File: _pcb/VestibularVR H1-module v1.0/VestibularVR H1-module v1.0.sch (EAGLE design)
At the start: 67 parts, among them IC1 FT232RL, IC2 74LVC1G07DBV, IC3 LP5907MFX-3.3, IC4 74LVC1G07DBV, IC5 74LVC1G07DBV, IC6 74LVC1G07DBV, IC7 USBLC6-2SC6, IC8 ATXMEGA32A4U, T1 DMG1012UW, T2 DMG1012UW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

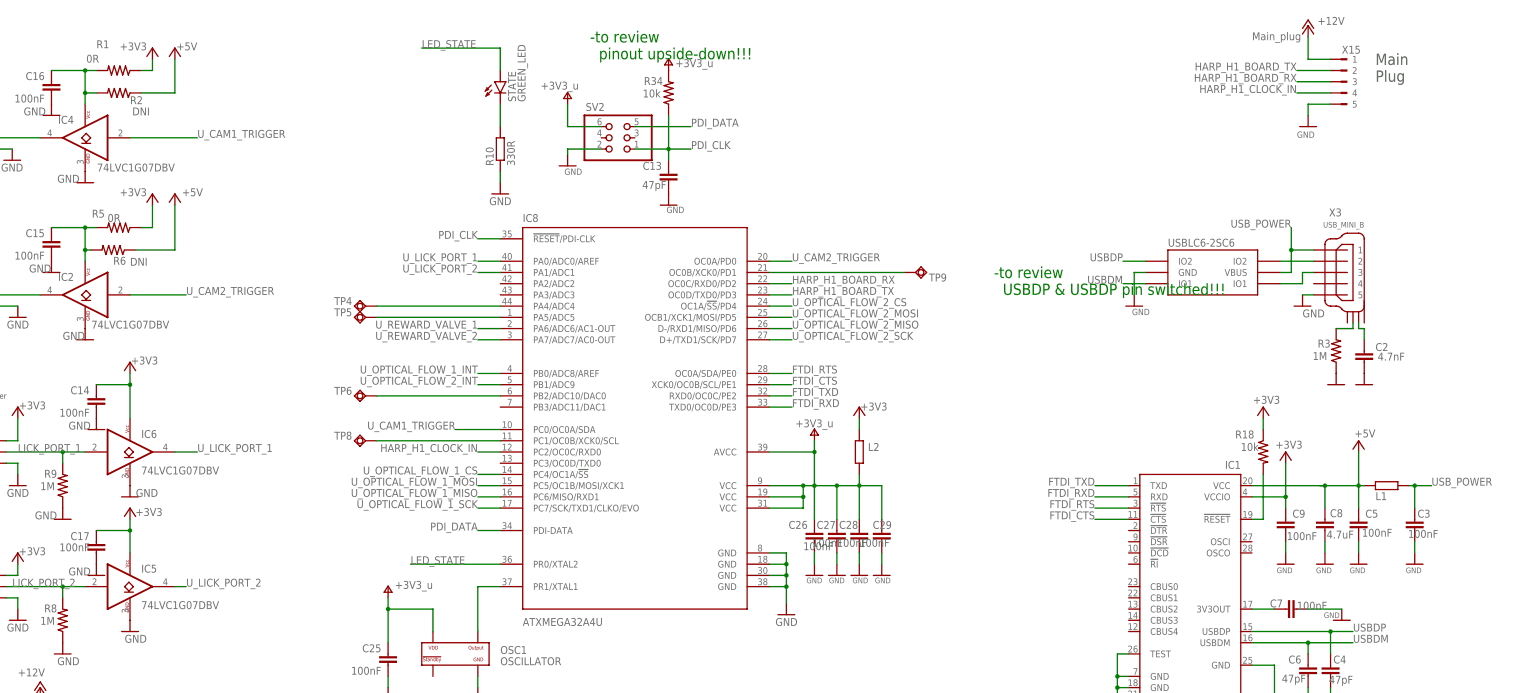
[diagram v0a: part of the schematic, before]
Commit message: VestibularVR H1BOM updates & Lick Sensor step on
- VestibularVR H1
. component ref updated
. BOM file updated

- Lick Sensor module v1.0
. still only on schematic design
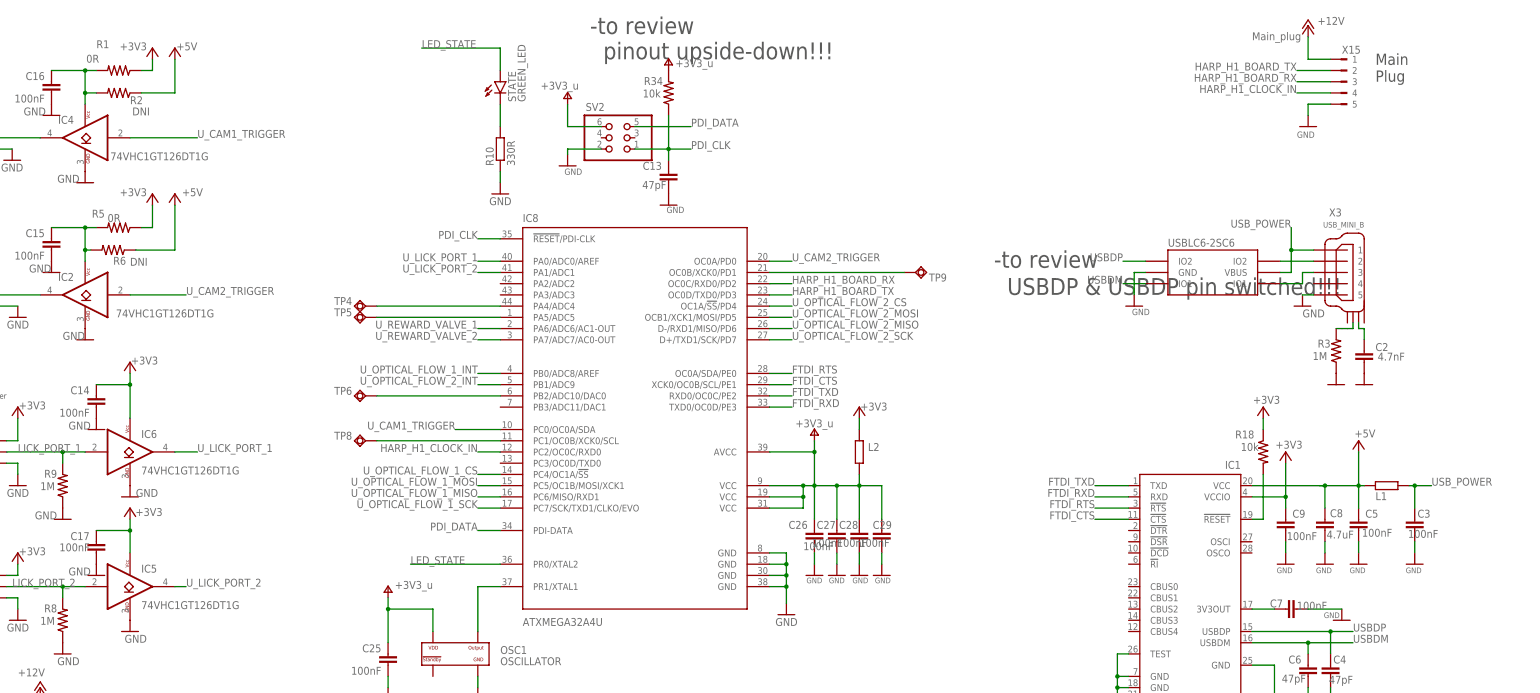
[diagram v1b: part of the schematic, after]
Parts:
- IC2, IC4, IC5, IC6: value 74LVC1G07DBV -> 74VHC1GT126DT1G
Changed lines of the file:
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@@
 <attribute name="OEPS" value="OEPS070015"/>
 </part>
-<part name="IC2" library="VestibularVR H1-module v1.0" deviceset="74LVC1G07" device="DBV" package3d_urn="urn:adsk.eagle:package:2406/2">
+<part name="IC2" library="VestibularVR H1-module v1.0" deviceset="74LVC1G07" device="DBV" package3d_urn="urn:adsk.eagle:package:2406/2" value="74VHC1GT126DT1G">
 <attribute name="MPN" value="M74VHC1GT126DT1G"/>
 <attribute name="OEPS" value="OEPS080017"/>
 </part>
-<part name="IC4" library="VestibularVR H1-module v1.0" deviceset="74LVC1G07" device="DBV" package3d_urn="urn:adsk.eagle:package:2406/2">
+<part name="IC4" library="VestibularVR H1-module v1.0" deviceset="74LVC1G07" device="DBV" package3d_urn="urn:adsk.eagle:package:2406/2" value="74VHC1GT126DT1G">
 <attribute name="MPN" value="M74VHC1GT126DT1G"/>
 <attribute name="OEPS" value="OEPS080017"/>
 </part>
-<part name="IC5" library="VestibularVR H1-module v1.0" deviceset="74LVC1G07" device="DBV" package3d_urn="urn:adsk.eagle:package:2406/2">
+<part name="IC5" library="VestibularVR H1-module v1.0" deviceset="74LVC1G07" device="DBV" package3d_urn="urn:adsk.eagle:package:2406/2" value="74VHC1GT126DT1G">
 <attribute name="MPN" value="M74VHC1GT126DT1G"/>
 <attribute name="OEPS" value="OEPS080017"/>
 </part>
-<part name="IC6" library="VestibularVR H1-module v1.0" deviceset="74LVC1G07" device="DBV" package3d_urn="urn:adsk.eagle:package:2406/2">
+<part name="IC6" library="VestibularVR H1-module v1.0" deviceset="74LVC1G07" device="DBV" package3d_urn="urn:adsk.eagle:package:2406/2" value="74VHC1GT126DT1G">
 <attribute name="MPN" value="M74VHC1GT126DT1G"/>
 <attribute name="OEPS" value="OEPS080017"/>
@@
 <text x="58.42" y="88.9" size="1.778" layer="91">DMG1012UW</text>
 <text x="55.88" y="38.1" size="1.778" layer="91">DMG1012UW</text>
-<text x="266.7" y="185.42" size="2.54" layer="91" font="vector" ratio="16">-to review
+<text x="266.7" y="185.42" size="3.81" layer="97" font="vector" ratio="16" distance="61">-to review
   USBDP &amp; USBDP pin switched!!!</text>
-<text x="175.26" y="238.76" size="2.54" layer="91" font="vector" ratio="16">-to review
+<text x="175.26" y="238.76" size="3.81" layer="97" font="vector" ratio="16">-to review
   pinout upside-down!!!</text>
 </plain>
@@
 <instance part="IC2" gate="A" x="60.96" y="185.42" smashed="yes" rot="MR0">
 <attribute name="NAME" x="58.42" y="188.595" size="1.778" layer="95" rot="MR0"/>
-<attribute name="VALUE" x="80.01" y="177.8" size="1.778" layer="96" rot="MR0"/>
+<attribute name="VALUE" x="90.17" y="180.34" size="1.778" layer="96" rot="MR0"/>
 <attribute name="MPN" x="60.96" y="185.42" size="1.778" layer="96" rot="MR0" display="off"/>
 <attribute name="OEPS" x="60.96" y="185.42" size="1.778" layer="96" rot="MR0" display="off"/>
@@
 <instance part="IC4" gate="A" x="60.96" y="220.98" smashed="yes" rot="MR0">
 <attribute name="NAME" x="58.42" y="224.155" size="1.778" layer="95" rot="MR0"/>
-<attribute name="VALUE" x="81.28" y="213.36" size="1.778" layer="96" rot="MR0"/>
+<attribute name="VALUE" x="88.9" y="215.9" size="1.778" layer="96" rot="MR0"/>
 <attribute name="MPN" x="60.96" y="220.98" size="1.778" layer="96" rot="MR0" display="off"/>
 <attribute name="OEPS" x="60.96" y="220.98" size="1.778" layer="96" rot="MR0" display="off"/>

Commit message: >> VestibularVR H1-module v1.0: corrected part numbers
>> VestibularVR H1-module v1.0
- notes added on schematic
	. buffers with wrong pn - corrected OEPS code; still wrong buffers' symbol
	generated new BOM with corrected pn
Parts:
- C13, C4, C6: OEPS OEPS080013 -> n.a.
- IC2, IC4, IC5, IC6: value 74VHC1GT126DT1G -> SN74LVC1G125DBVT; MPN M74VHC1GT126DT1G -> SN74LVC1G125DBVT; OEPS OEPS080017 -> OEPS080029
- X1: MPN 2x5 header -> (none)
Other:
- note added: "- to review IC2, IC4, IC5, IC6 part nb corrected: - was set as 74VHC1GT126DT1G - was changed to SN74LVC1G125DBVT - both parts have Enable pin; pin not drawn in symbol - new part SN74LVC1G125DBVT more available in suppliers - Enable pin of 74VHC1GT126DT1G active high; - Enable pin of new SN74LVC1G125DBVT active low; > more safe; independent of voltage supply used - part number corrected - OEPS cod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"
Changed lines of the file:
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@@
 <attribute name="OEPS" value="OEPS070015"/>
 </part>
-<part name="IC2" library="VestibularVR H1-module v1.0" deviceset="74LVC1G07" device="DBV" package3d_urn="urn:adsk.eagle:package:2406/2" value="74VHC1GT126DT1G">
-<attribute name="MPN" value="M74VHC1GT126DT1G"/>
-<attribute name="OEPS" value="OEPS080017"/>
-</part>
-<part name="IC4" library="VestibularVR H1-module v1.0" deviceset="74LVC1G07" device="DBV" package3d_urn="urn:adsk.eagle:package:2406/2" value="74VHC1GT126DT1G">
-<attribute name="MPN" value="M74VHC1GT126DT1G"/>
-<attribute name="OEPS" value="OEPS080017"/>
-</part>
-<part name="IC5" library="VestibularVR H1-module v1.0" deviceset="74LVC1G07" device="DBV" package3d_urn="urn:adsk.eagle:package:2406/2" value="74VHC1GT126DT1G">
-<attribute name="MPN" value="M74VHC1GT126DT1G"/>
-<attribute name="OEPS" value="OEPS080017"/>
-</part>
-<part name="IC6" library="VestibularVR H1-module v1.0" deviceset="74LVC1G07" device="DBV" package3d_urn="urn:adsk.eagle:package:2406/2" value="74VHC1GT126DT1G">
-<attribute name="MPN" value="M74VHC1GT126DT1G"/>
-<attribute name="OEPS" value="OEPS080017"/>
+<part name="IC2" library="VestibularVR H1-module v1.0" deviceset="74LVC1G07" device="DBV" package3d_urn="urn:adsk.eagle:package:2406/2" value="SN74LVC1G125DBVT">
+<attribute name="MPN" value="SN74LVC1G125DBVT"/>
+<attribute name="OEPS" value="OEPS080029"/>
+</part>
+<part name="IC4" library="VestibularVR H1-module v1.0" deviceset="74LVC1G07" device="DBV" package3d_urn="urn:adsk.eagle:package:2406/2" value="SN74LVC1G125DBVT">
+<attribute name="MPN" value="SN74LVC1G125DBVT"/>
+<attribute name="OEPS" value="OEPS080029"/>
+</part>
+<part name="IC5" library="VestibularVR H1-module v1.0" deviceset="74LVC1G07" device="DBV" package3d_urn="urn:adsk.eagle:package:2406/2" value="SN74LVC1G125DBVT">
+<attribute name="MPN" value="SN74LVC1G125DBVT"/>
+<attribute name="OEPS" value="OEPS080029"/>
+</part>
+<part name="IC6" library="VestibularVR H1-module v1.0" deviceset="74LVC1G07" device="DBV" package3d_urn="urn:adsk.eagle:package:2406/2" value="SN74LVC1G125DBVT">
+<attribute name="MPN" value="SN74LVC1G125DBVT"/>
+<attribute name="OEPS" value="OEPS080029"/>
 </part>
 <part name="GND65" library="supply1" deviceset="GND" device=""/>
@@
 <part name="C4" library="rcl" library_urn="urn:adsk.eagle:library:334" deviceset="C-EU" device="C0402K" package3d_urn="urn:adsk.eagle:package:23679/2" value="47pF">
 <attribute name="MPN" value="04025A470JAT2A"/>
-<attribute name="OEPS" value="OEPS080013"/>
+<attribute name="OEPS" value="n.a."/>
 </part>
 <part name="C6" library="rcl" library_urn="urn:adsk.eagle:library:334" deviceset="C-EU" device="C0402K" package3d_urn="urn:adsk.eagle:package:23679/2" value="47pF">
 <attribute name="MPN" value="04025A470JAT2A"/>
-<attribute name="OEPS" value="OEPS080013"/>
+<attribute name="OEPS" value="n.a."/>
 </part>
 <part name="L1" library="rcl" library_urn="urn:adsk.eagle:library:334" deviceset="R-EU_" device="R0603" package3d_urn="urn:adsk.eagle:package:23555/3" value="40R@100MHz">
@@
 <part name="C13" library="rcl" library_urn="urn:adsk.eagle:library:334" deviceset="C-EU" device="C0402K" package3d_urn="urn:adsk.eagle:package:23679/2" value="47pF">
 <attribute name="MPN" value="04025A470JAT2A"/>
-<attribute name="OEPS" value="OEPS080013"/>
+<attribute name="OEPS" value="n.a."/>
 </part>
 <part name="R8" library="rcl" library_urn="urn:adsk.eagle:library:334" deviceset="R-US_" device="R0402" package3d_urn="urn:adsk.eagle:package:23547@1/3" value="1M">
@@
 </part>
 <part name="X1" library="con-samtec" library_urn="urn:adsk.eagle:library:184" deviceset="TSW-105-02-S-D" device="" value="2x5 header">
-<attribute name="MPN" value="2x5 header"/>
 <attribute name="OEPS" value="n.a."/>
 </part>
@@
 Plug</text>
 <text x="111.76" y="60.96" size="2.54" layer="97" font="vector" ratio="15">Optical Flows</text>
-<text x="134.62" y="-17.78" size="1.778" layer="91">&gt; 6 pins flat cable.. som3?? Should we change header
-https://eu.mouser.com/c/connectors/headers-wire-housings/?mounting%20style=Through%20Hole&amp;number%20of%20positions=8%20Position&amp;number%20of%20rows=2%20Row&amp;pitch=2.54%20mm&amp;row%20spacing=2.54%20mm&amp;instock=y
-https://eu.mouser.com/ProductDetail/Molex/70246-0804?qs=UkDUCjYnTB3Qq7EFSr2OxA%3D%3D</text>
 <text x="7.62" y="134.62" size="2.1844" layer="91">Lick port de OC
 maior R PDown ~50k</text>
@@
 <text x="175.26" y="238.76" size="3.81" layer="97" font="vector" ratio="16">-to review
   pinout upside-down!!!</text>
+<text x="22.86" y="238.76" size="2.1844" layer="97" font="vector" ratio="17">- to review
+IC2, IC4, IC5, IC6 part nb corrected:
+- was set as 74VHC1GT126DT1G
+- was changed to SN74LVC1G125DBVT
+- both parts have Enable pin; pin not drawn in symbol
+- new part SN74LVC1G125DBVT more available in suppliers
+- Enable pin of 74VHC1GT126DT1G active high;
+- Enable pin of new SN74LVC1G125DBVT active low;
+&gt; more safe; independent of voltage supply used
+- part number corrected
+- OEPS code corrected
+- symbol draw not corrected
+- new BOM generated
+</text>
 </plain>
 <instances>
